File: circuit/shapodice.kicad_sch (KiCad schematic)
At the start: 22 parts, among them Q1 2SC1815, SW1 START, SW2 MUTE, U1 ATtiny85-20P

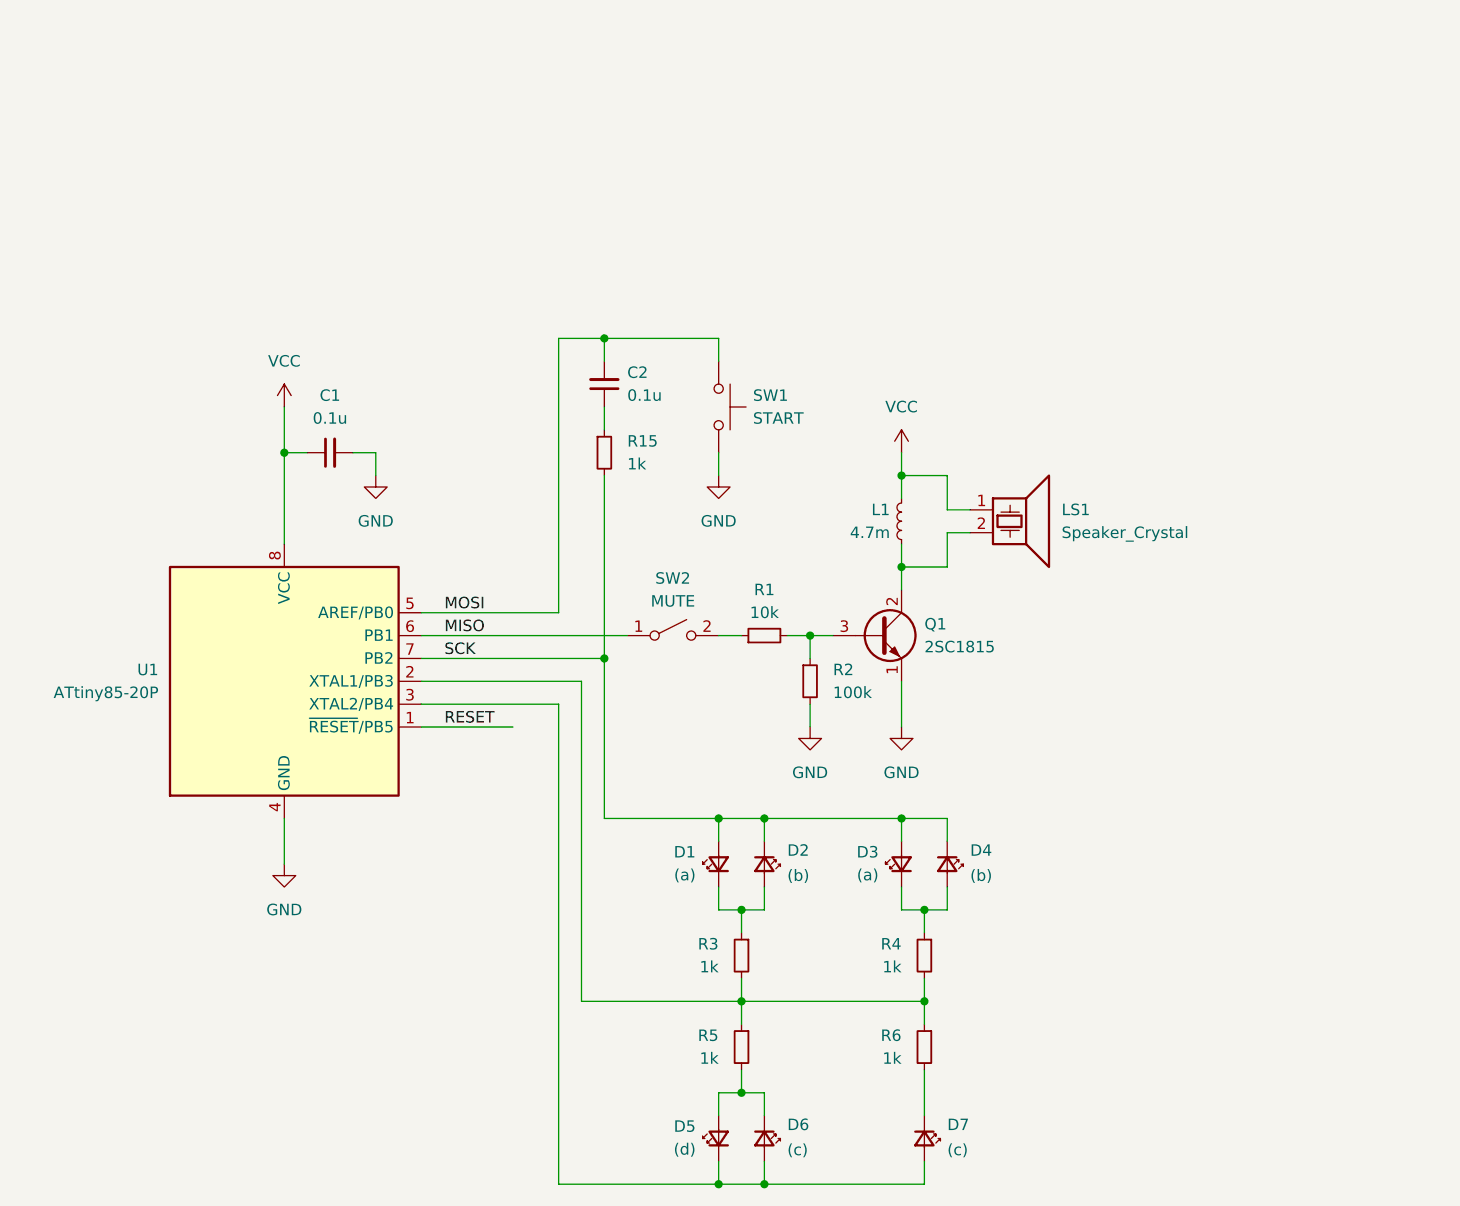
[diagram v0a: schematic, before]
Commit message: add low battery indicator (2074B)
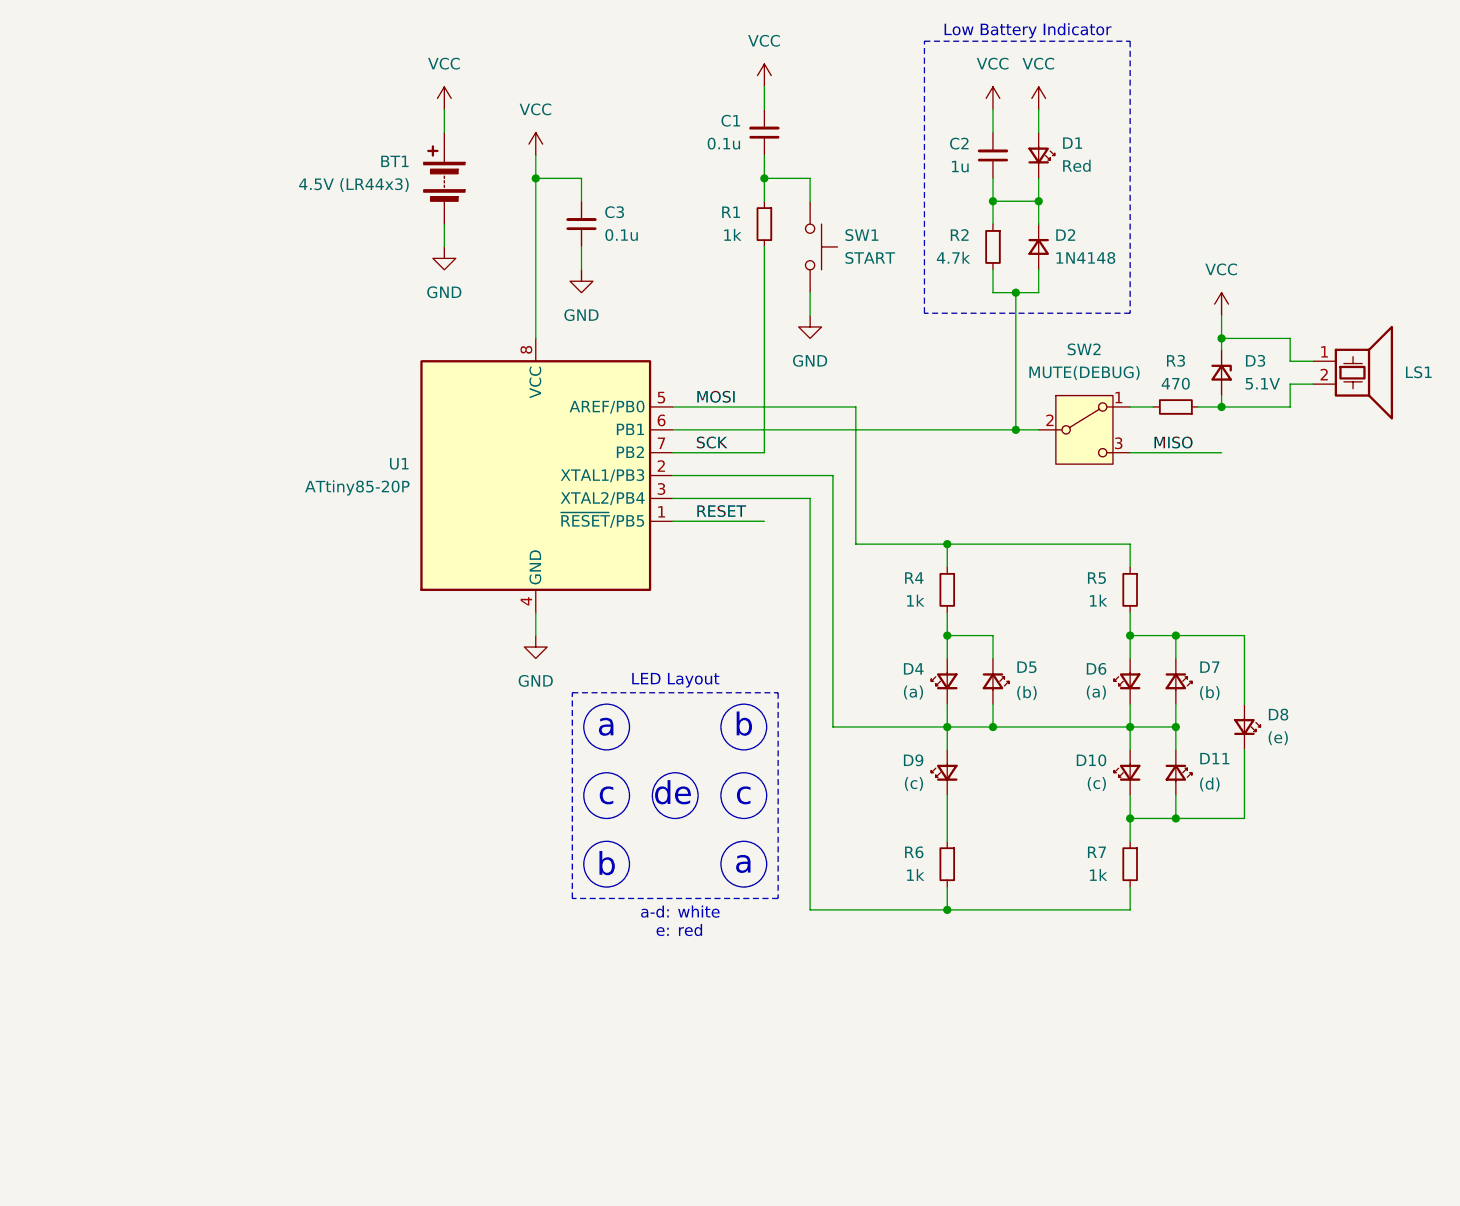
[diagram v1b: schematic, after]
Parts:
- removed D2: (b), symbol Device:LED_Small
- removed D3: (a), symbol Device:LED_Small
- removed L1: 4.7m, symbol Device:L_Small
- removed Q1: 2SC1815, Package_TO_SOT_THT:TO-92_Inline, symbol Transistor_BJT:2SC1815
- removed R15: 1k, symbol Device:R_Small
- removed SW2: MUTE, symbol Switch:SW_SPST
- added BT1: 4.5V (LR44x3), symbol Device:Battery
- added C3: 0.1u, symbol Device:C_Small
- added D10, D9: (c), symbol Device:LED_Small
- added D11: (d), symbol Device:LED_Small
- added D2: 1N4148, symbol Device:D_Small
- added D3: 5.1V, symbol Device:D_Zener_Small
- added D8: (e), symbol Device:LED_Small
- added R7: 1k, symbol Device:R_Small
- added SW2: MUTE(DEBUG), symbol Switch:SW_SPDT
- C2: value 0.1u -> 1u
- D1: value (a) -> Red
- D4: value (b) -> (a)
- D5: value (d) -> (b)
- D6: value (c) -> (a)
- D7: value (c) -> (b)
- R1: value 10k -> 1k
- R2: value 100k -> 4.7k
- R3: value 1k -> 470
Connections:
- net GND: now also BT1.2 (-), C3.1; no longer C1.2, R2.2
- net MISO: now also SW2.3 (C); no longer U1.6 (PB1)
- net MOSI: now also R4.1, R5.1; no longer C2.2, SW1.2
- net SCK: now also R1.2; no longer D1.2 (A), D4.1 (K)
- net VCC: now also C1.2, C2.2, D1.2 (A), BT1.1 (+), C3.2, D3.1 (K); no longer C1.1
- net at C2.1: now also D1.1 (K), R2.1, D2.1 (K)
- net at D5.2 (A), D6.1 (K): now also D4.1 (K), D7.2 (A), U1.2 (XTAL1/PB3), D10.2 (A), D11.1 (K), D9.2 (A); no longer R5.2
- net at D4.2 (A): now also D5.1 (K), R4.2; no longer R4.1
- net at LS1.2: now also R3.1, D3.2 (A)
- net at D7.1 (K): now also D6.2 (A), R5.2, D8.2 (A); no longer R6.2
- net at R1.1: now also C1.1, SW1.2
- new net: D10.1 (K), D11.2 (A), D8.1 (K), R7.1
- new net: D2.2 (A), R2.2, SW2.2 (B), U1.6 (PB1)
- new net: R3.2, SW2.1 (A)
- new net: R6.2, R7.2, U1.3 (XTAL2/PB4)
- new net: D9.1 (K), R6.1
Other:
- note added: "LED Layout"
- note added: "Low Battery Indicator"
- note added: "a"
- note added: "a-d: e:"
- note added: "b"
- note added: "c"
- note added: "de"
- note added: "white red"
- moved on the sheet: U1

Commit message: fix LED layout (2066B)
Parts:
- removed C2: 1u, symbol Device:C_Small
- removed D1: Red, symbol Device:LED_Small
- removed D2: 1N4148, symbol Device:D_Small
- removed R2: 4.7k, symbol Device:R_Small
- added D12: (f), symbol Device:LED_Small
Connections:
- net at D6.2 (A), D7.1 (K), D8.2 (A)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: now also D12.1 (K)
- net at D10.1 (K), D11.2 (A), D8.1 (K)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: now also D12.2 (A)
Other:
- note added: "Dice LEDs"
- note added: "a-d: e-f:"
- note added: "f"
- note removed: "LED Layout"
- note removed: "a-d: e:"
- moved on the sheet: D3, D8, LS1, R3, SW2

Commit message: fix schematic
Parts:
- removed R1: 1k, symbol Device:R_Small
- added R7: 1k, symbol Device:R_Small
- C2: renamed from C3; value 0.1u -> 1u
- R3: renamed from R4; value 1k -> 470
- R4: renamed from R5; value 1k -> 470
- R5: renamed from R6; value 1k -> 470
- R6: renamed from R7; value 1k -> 470
- renumbered D3 to D1, D11 to D10, D4 to D2, D5 to D3, D6 to D4, D7 to D5, D8 to D6, D12 to D7, D9 to D8, D10 to D9, R3 to R2
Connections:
- net GND: now also SW1.2; no longer SW1.1
- net SCK: now also C1.1, R7.2
- new net: R7.1, SW1.1
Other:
- moved on the sheet: C1

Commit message: circuit simplified
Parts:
- removed C1: 0.1u, symbol Device:C_Small
- removed R7: 1k, symbol Device:R_Small
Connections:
- net SCK: now also SW1.1
- net at D1.2 (A), LS1.2: now also SW2.1 (A); no longer R2.1
- net at R2.2: now also U1.6 (PB1); no longer SW2.1 (A)
- net at SW2.2 (B): now also R2.1; no longer U1.6 (PB1)
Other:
- moved on the sheet: R2, SW1, SW2

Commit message: fix README
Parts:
- removed C2: 1u, symbol Device:C_Small
- added C1: 1u, symbol Device:C_Small
- BT1: value 4.5V (LR44x3) -> 4.5V (3x LR44)
- renumbered R2 to R1, R3 to R2, R4 to R3, R5 to R4, R6 to R5
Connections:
- net GND: now also C1.2
- net MISO: now also U1.6 (PB1)
- net VCC: now also C1.1
- net at D1.2 (A), LS1.2: now also R1.1; no longer SW2.1 (A)
- net at SW2.2 (B): now also R1.2; no longer R1.1
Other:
- note added: "d"
- note added: "e"
- note removed: "de"
- moved on the sheet: BT1, D10, D2, D3, D4, D5, D6, D7, D8, D9, R1, R2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
